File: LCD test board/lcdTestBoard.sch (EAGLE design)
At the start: 77 parts, among them CON2 AXE534124, IC1 4069D, U1 LP2980-ADJ, U10 TPS63030DSKT, U2 ST2378E_TSSOP, U3 MCP1662, U4 TPS62260, U5 ST2378E_TSSOP, U6 LP2980-ADJ, U7 TPS62260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

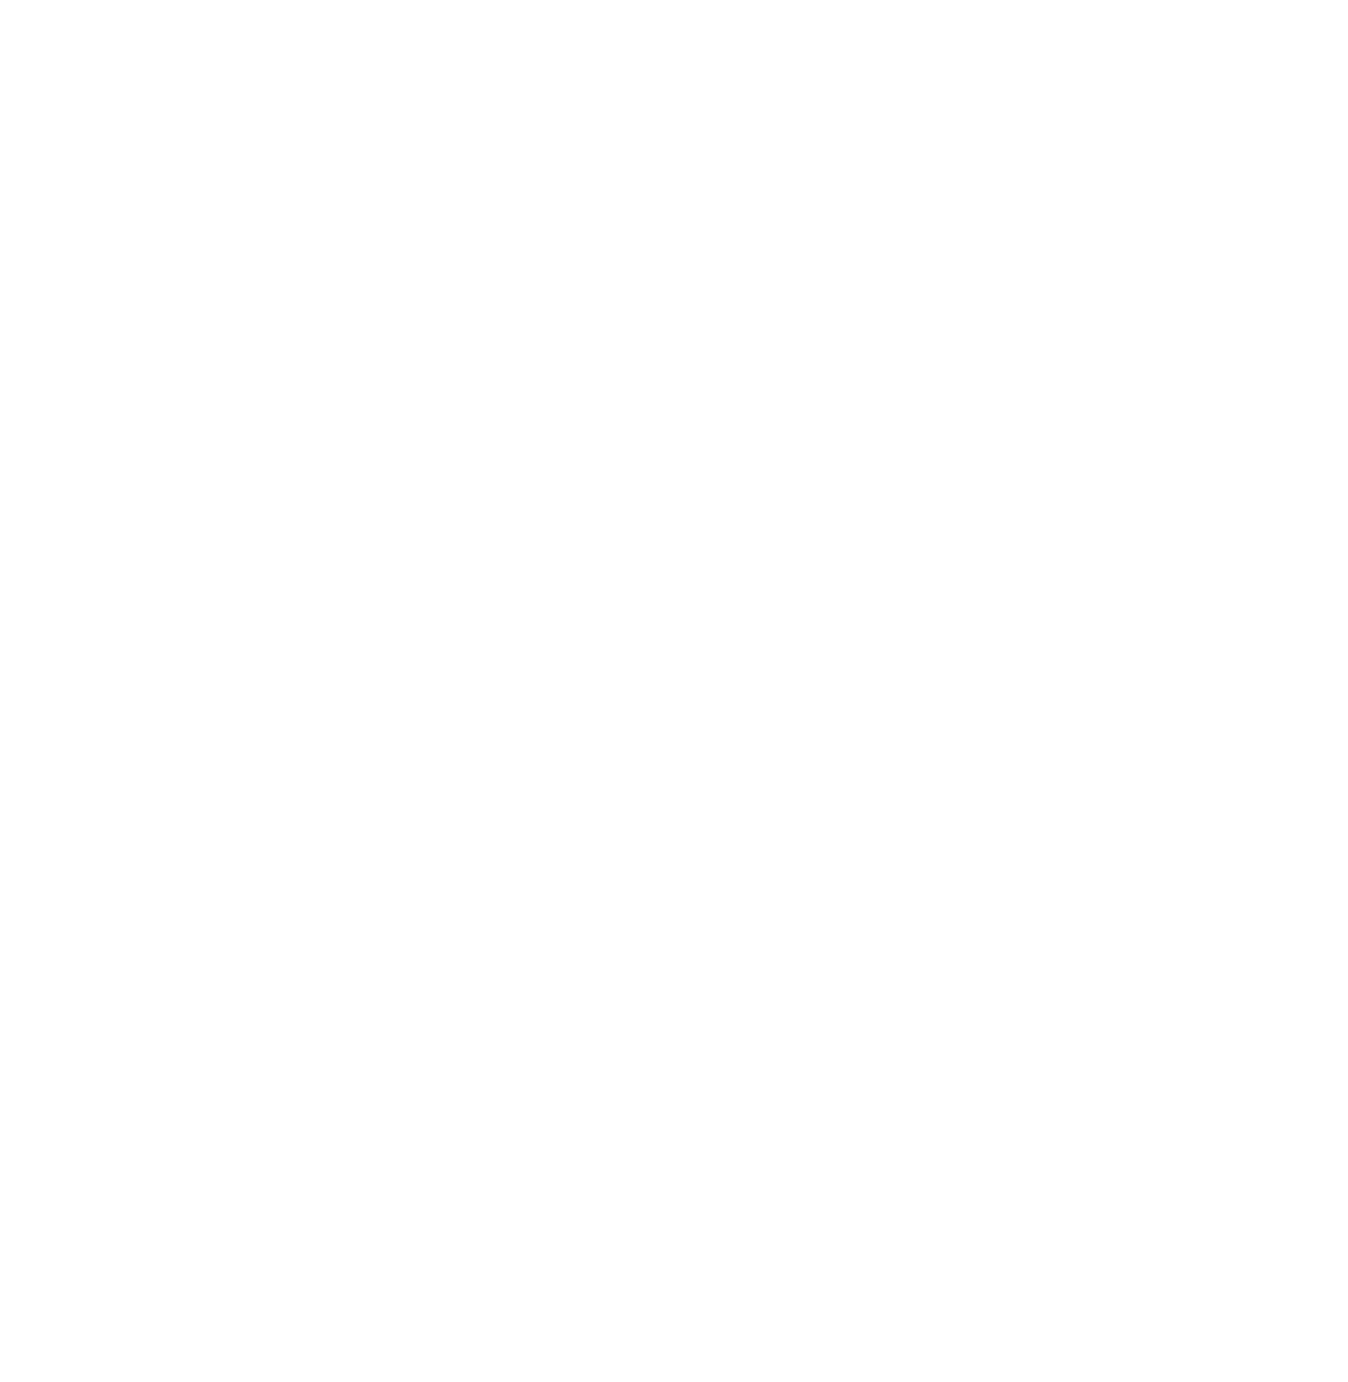
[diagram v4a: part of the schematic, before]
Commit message: Dodano pojemnościowy kontroler panelu dotykowego
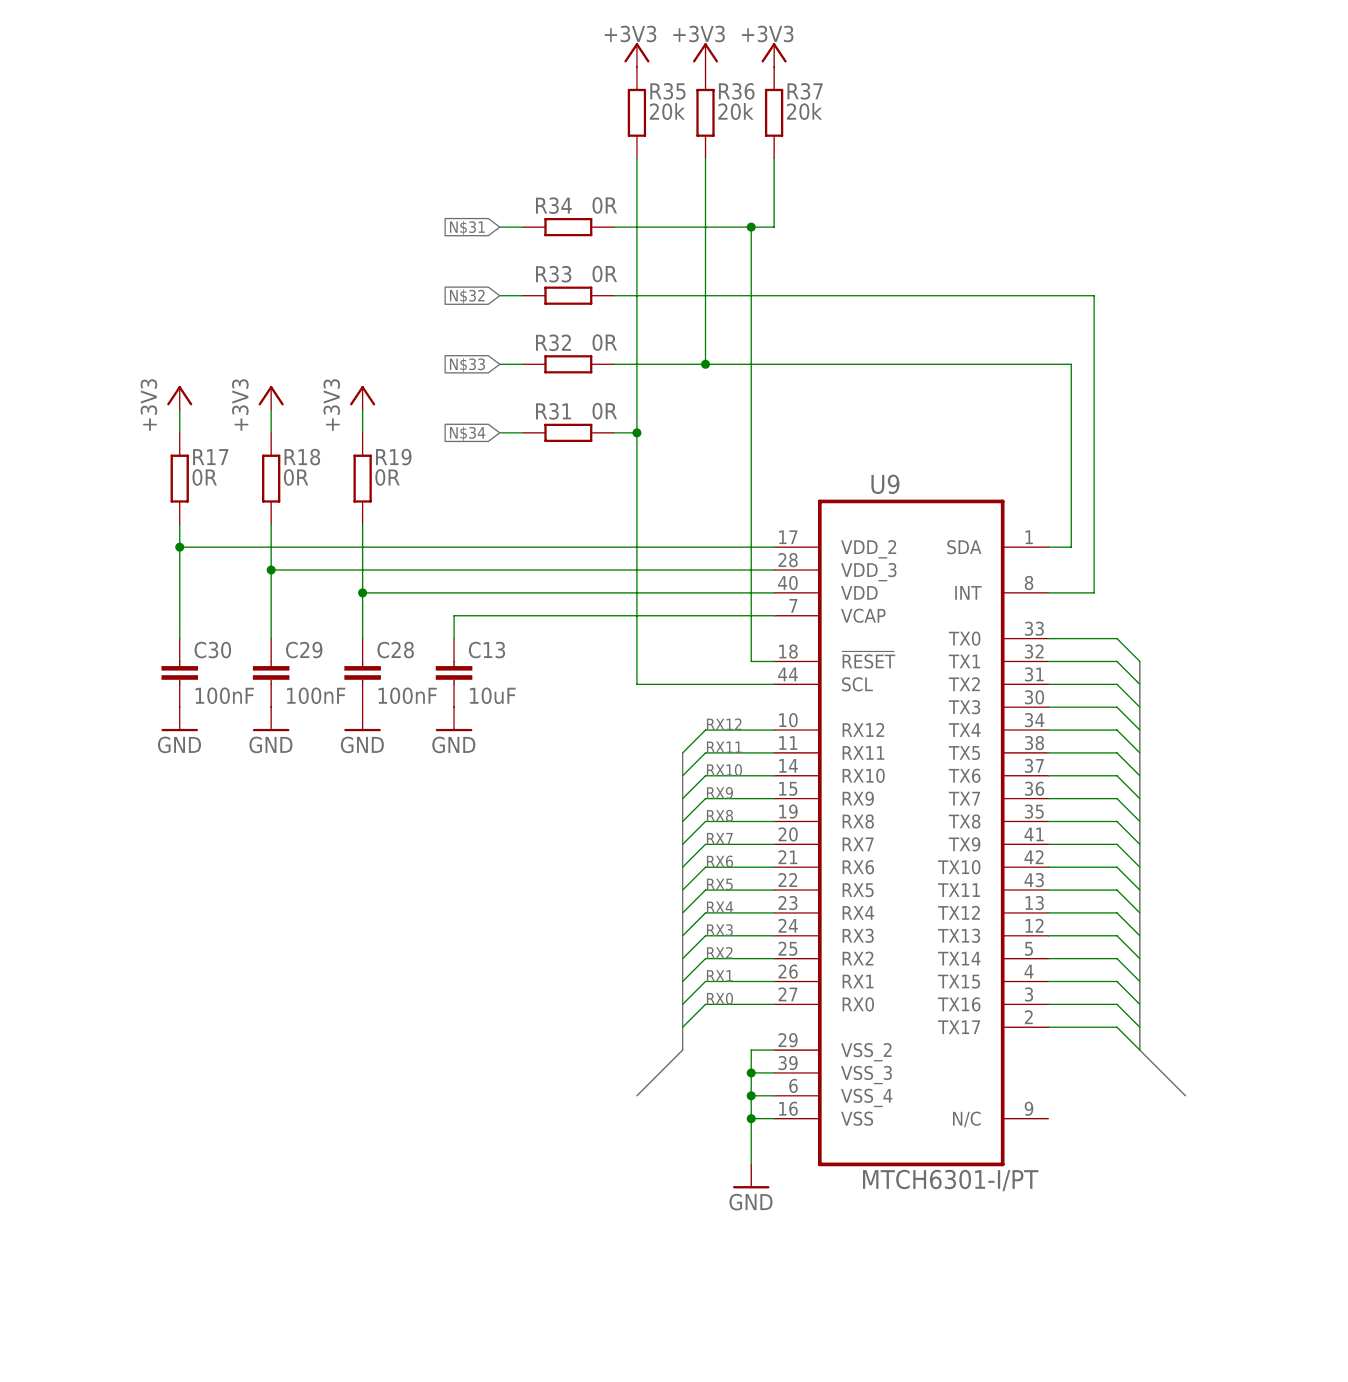
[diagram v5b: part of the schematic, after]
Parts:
- added C13: 10uF, rcl:C-EUC0603K
- added C28, C29, C30: 100nF, rcl:C-EUC0603K
- added R17, R18, R19, R31, R32, R33, R34: 0R, rcl:R-EU_R0603
- added R35, R36, R37: 20k, rcl:R-EU_R0603
- added U9: MTCH6301-I/PT, mtch6301:MTCH6301-I/PT
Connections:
- new net N$22: C13.1, U9.VCAP
- new net N$24: C28.1, R19.2, U9.VDD
- new net N$25: C29.1, R18.2, U9.VDD_3
- new net N$26: C30.1, R17.2, U9.VDD_2
- new net N$27: R31.1, R35.2, U9.SCL
- new net N$28: R34.1, R37.2, U9.!RESET
- new net N$29: R32.1, R36.2, U9.SDA
- new net N$30: R33.1, U9.INT
- new net N$31: R34.2
- new net N$32: R33.2
- new net N$33: R32.2
- new net N$34: R31.2
- new net RX0: U9.RX0
- new net RX1: U9.RX1
- new net RX10: U9.RX10
- new net RX11: U9.RX11
- new net RX12: U9.RX12
- new net RX2: U9.RX2
- new net RX3: U9.RX3
- new net RX4: U9.RX4
- new net RX5: U9.RX5
- new net RX6: U9.RX6
- new net RX7: U9.RX7
- new net RX8: U9.RX8
- new net RX9: U9.RX9
- new net TX0: U9.TX0
- new net TX1: U9.TX1
- new net TX10: U9.TX10
- new net TX11: U9.TX11
- new net TX12: U9.TX12
- new net TX13: U9.TX13
- new net TX14: U9.TX14
- new net TX15: U9.TX15
- new net TX16: U9.TX16
- new net TX17: U9.TX17
- new net TX2: U9.TX2
- new net TX3: U9.TX3
- new net TX4: U9.TX4
- new net TX5: U9.TX5
- new net TX6: U9.TX6
- new net TX7: U9.TX7
- new net TX8: U9.TX8
- new net TX9: U9.TX9
- net +3V3: now also R17.1, R18.1, R19.1, R35.1, R36.1, R37.1
- net GND: now also C13.2, C28.2, C29.2, C30.2, U9.VSS, U9.VSS_2, U9.VSS_3, U9.VSS_4

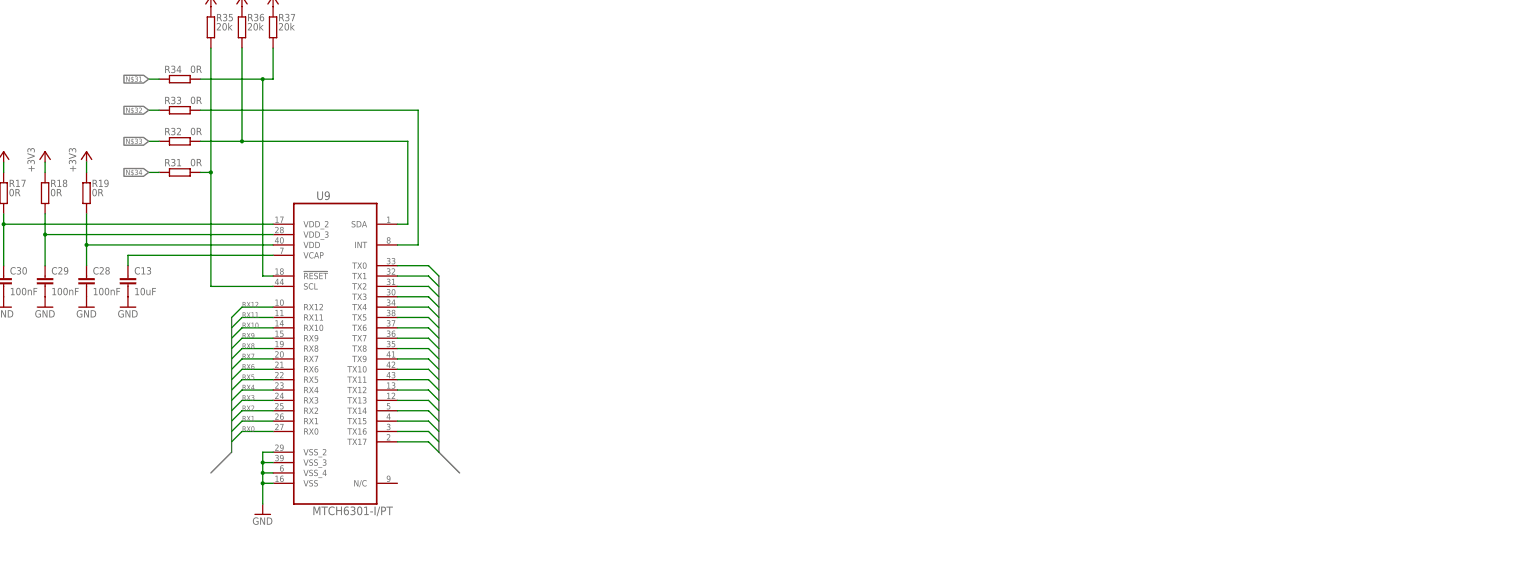
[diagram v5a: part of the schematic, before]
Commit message: added resistive touch panel controller
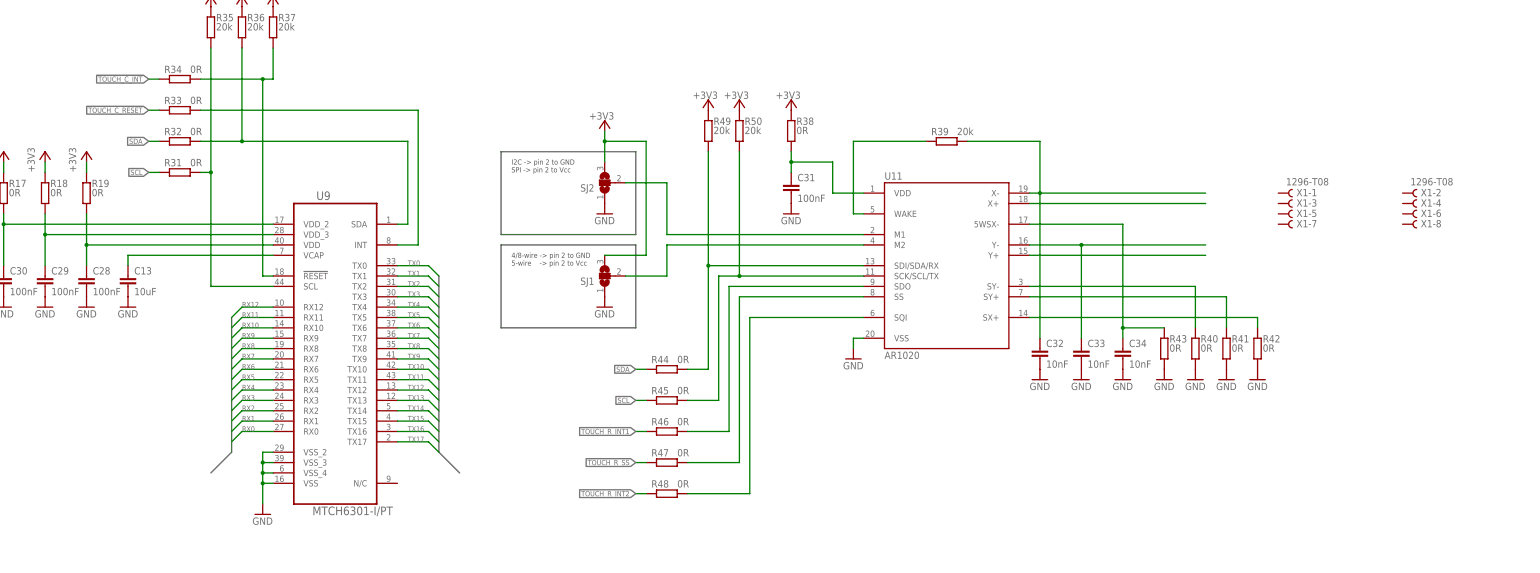
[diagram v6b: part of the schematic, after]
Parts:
- added C31: 100nF, rcl:C-EUC0603K
- added C32, C33, C34: 10nF, rcl:C-EUC0603K
- added R38, R40, R41, R42, R43, R44, R45, R46, R47, R48: 0R, rcl:R-EU_R0603
- added R39, R49, R50: 20k, rcl:R-EU_R0603
- added SJ1, SJ2: (no value), jumper:SJ2W
- added U11: AR1020, AR1020:AR1020
- added X1: 1296-T08, con-leotronics:1296-T08
- C13: device rcl:C-EUC0603K -> rcl:C-EUC1206K
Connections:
- net N$31 renamed TOUCH_C_INT
- net N$32 renamed TOUCH_C_RESET
- removed net N$33: R32.2
- removed net N$34: R31.2
- new net N$35: C31.1, R38.2, U11.VDD
- new net N$36: R39.2, U11.WAKE
- new net N$37: C32.1, R39.1, U11.X-
- new net N$38: C33.1, U11.Y-
- new net N$39: C34.1, R43.1, U11.5WSX-
- new net N$40: U11.X+
- new net N$41: U11.Y+
- new net N$42: R40.1, U11.SY-
- new net N$43: R41.1, U11.SY+
- new net N$44: R42.1, U11.SX+
- new net N$45: SJ2.2, U11.M1
- new net N$46: SJ1.2, U11.M2
- new net N$48: R44.1, R49.2, U11.SDI/SDA/RX
- new net N$49: R45.1, R50.2, U11.SCK/SCL/TX
- new net N$50: R46.1, U11.SDO
- new net N$51: R47.1, U11.SS
- new net N$52: R48.1, U11.SQI
- new net SCL: R31.2, R45.2
- new net SDA: R32.2, R44.2
- new net TOUCH_R_INT1: R46.2
- new net TOUCH_R_INT2: R48.2
- new net TOUCH_R_SS: R47.2
- net +3V3: now also R38.1, R49.1, R50.1, SJ1.3, SJ2.3
- net GND: now also C31.2, C32.2, C33.2, C34.2, R40.2, R41.2, R42.2, R43.2, SJ1.1, SJ2.1, U11.VSS
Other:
- note added: "4/8-wire -> pin 2 to GND 5-wire -> pin 2 to Vcc"
- note added: "I2C -> pin 2 to GND SPI -> pin 2 to Vcc"

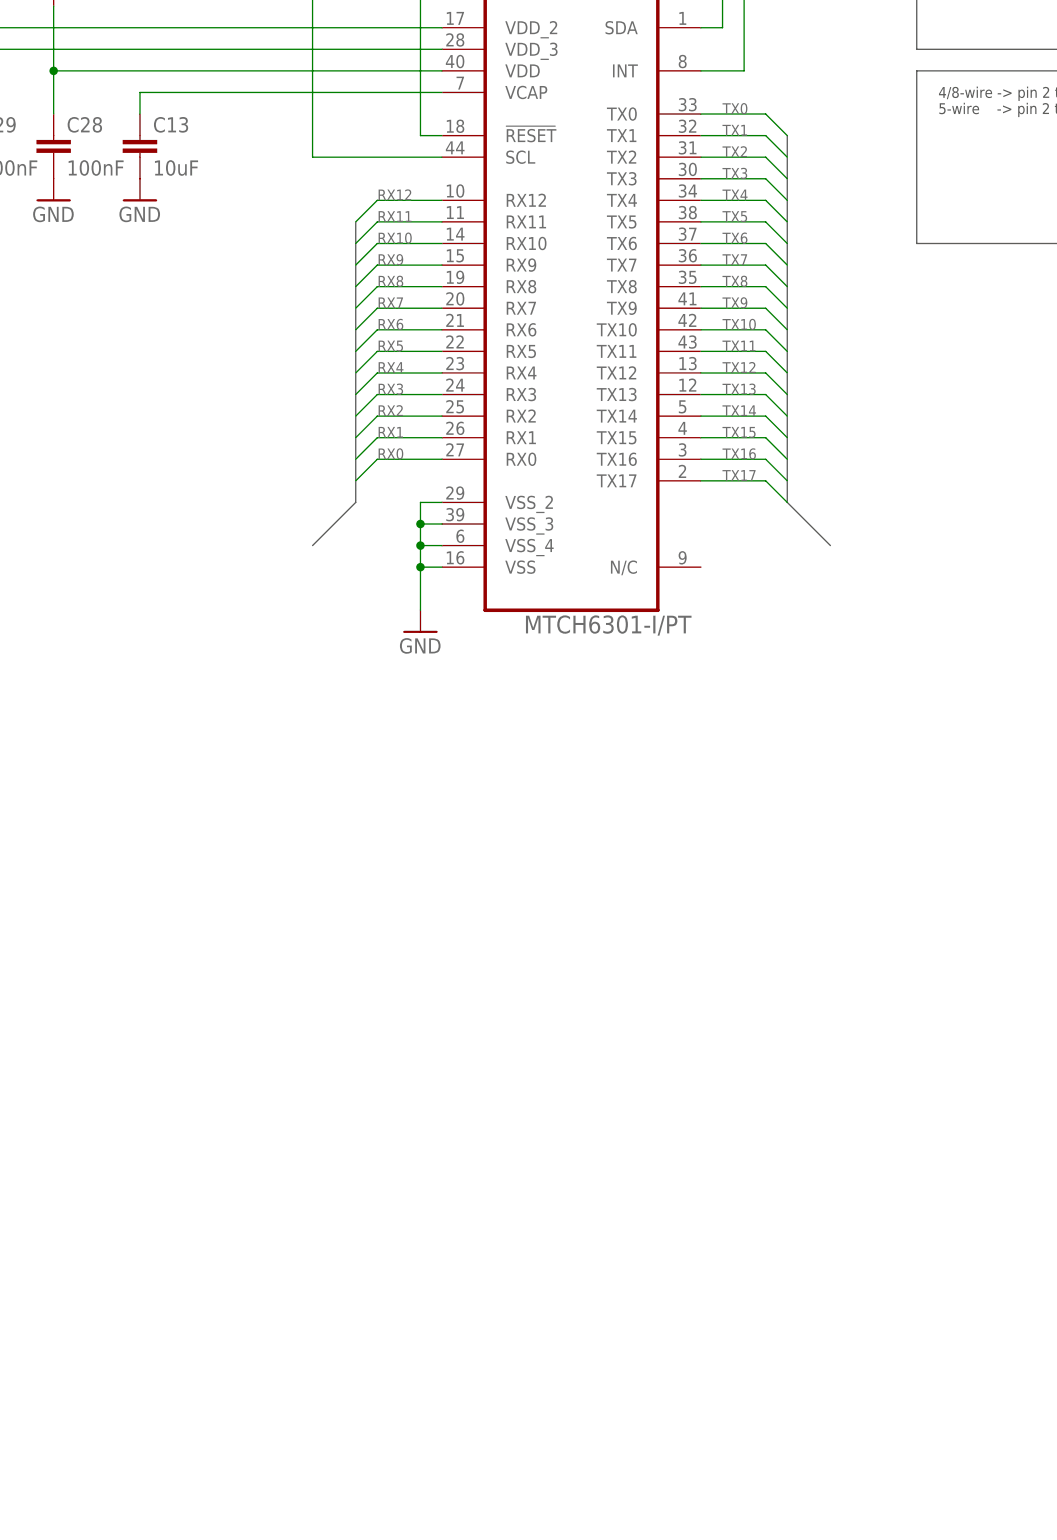
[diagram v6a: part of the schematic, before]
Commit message: added touch panel connectors
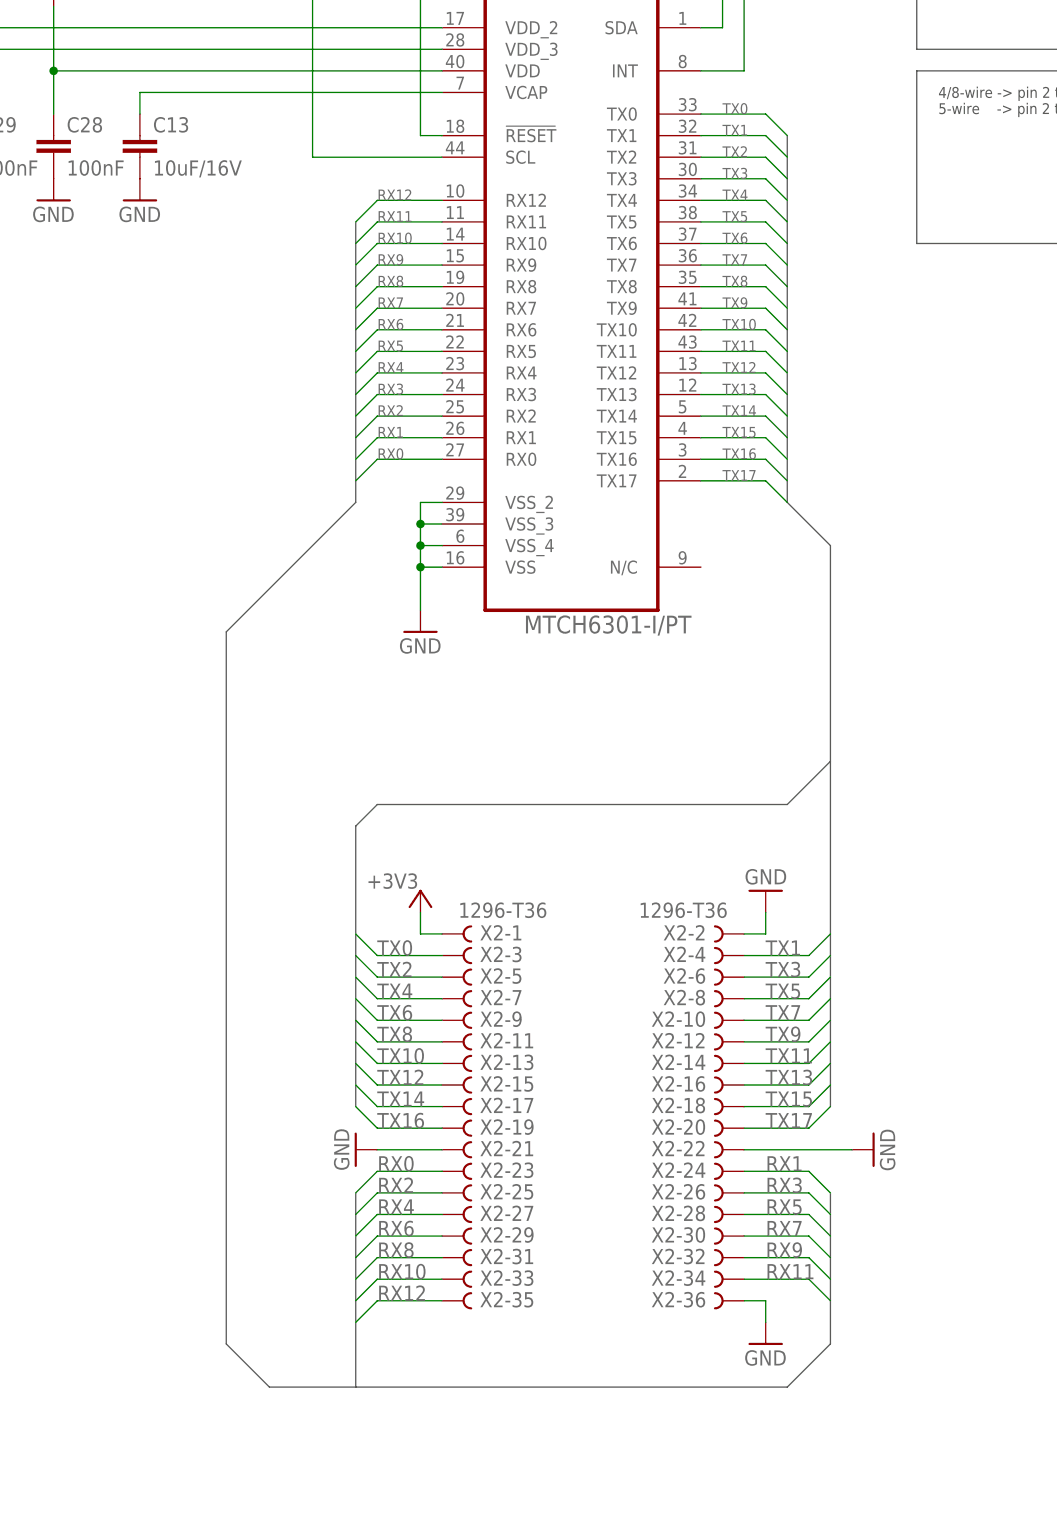
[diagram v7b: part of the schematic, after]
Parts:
- added X2: 1296-T36, con-leotronics:1296-T36
- C13: value 10uF -> 10uF/16V
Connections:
- net +3V3: now also X2-1.B
- net GND: now also X2-2.B, X2-21.B, X2-22.B, X2-36.B
- net RX0: now also X2-23.B
- net RX1: now also X2-24.B
- net RX10: now also X2-33.B
- net RX11: now also X2-34.B
- net RX12: now also X2-35.B
- net RX2: now also X2-25.B
- net RX3: now also X2-26.B
- net RX4: now also X2-27.B
- net RX5: now also X2-28.B
- net RX6: now also X2-29.B
- net RX7: now also X2-30.B
- net RX8: now also X2-31.B
- net RX9: now also X2-32.B
- net TX0: now also X2-3.B
- net TX1: now also X2-4.B
- net TX10: now also X2-13.B
- net TX11: now also X2-14.B
- net TX12: now also X2-15.B
- net TX13: now also X2-16.B
- net TX14: now also X2-17.B
- net TX15: now also X2-18.B
- net TX16: now also X2-19.B
- net TX17: now also X2-20.B
- net TX2: now also X2-5.B
- net TX3: now also X2-6.B
- net TX4: now also X2-7.B
- net TX5: now also X2-8.B
- net TX6: now also X2-9.B
- net TX7: now also X2-10.B
- net TX8: now also X2-11.B
- net TX9: now also X2-12.B
